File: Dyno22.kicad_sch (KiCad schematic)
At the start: 45 parts, among them J1 Pwr Input, J2 Display, J3 Pwr Output, J4 BPM & Sensors, J7 UART, U1 TS2937CW50, U2 LM324, U3 Demux

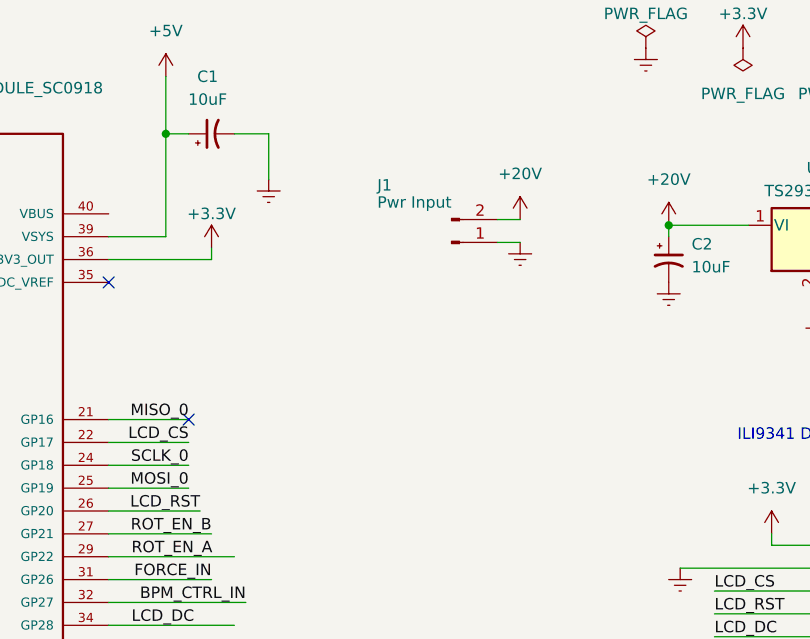
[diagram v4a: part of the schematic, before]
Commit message: Schematic modifications, including additional switch, fuse and LED
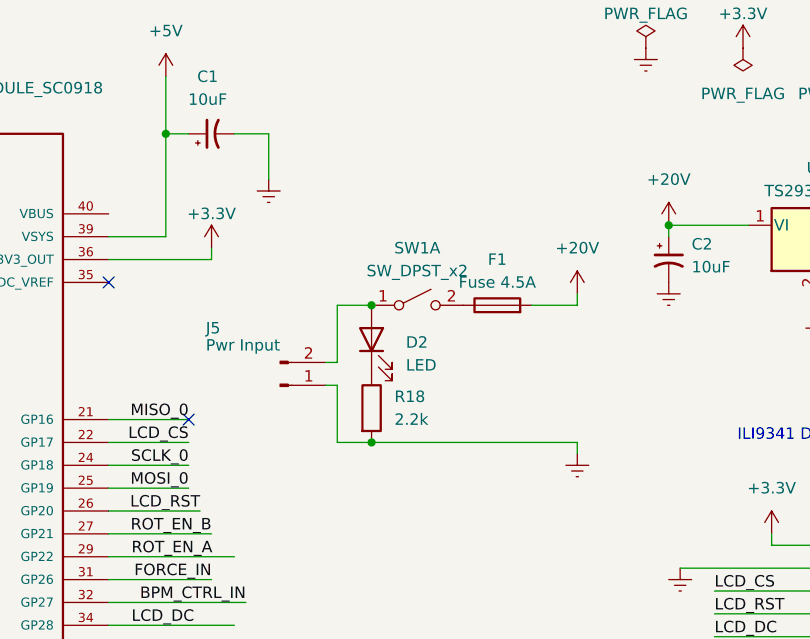
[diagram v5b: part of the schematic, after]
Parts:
- removed J1: Pwr Input, Connector_Molex:Molex_Nano-Fit_105313-xx02_1x02_P2.50mm_Horizontal, symbol Connector:Conn_01x02_Male
- added D2: LED, LED_SMD:LED_0603_1608Metric, symbol Device:LED
- added F1: Fuse 4.5A, symbol Device:Fuse
- added J5: Pwr Input, Connector_Molex:Molex_Nano-Fit_105313-xx02_1x02_P2.50mm_Horizontal, symbol Connector:Conn_01x02_Male
- added R18: 2.2k, Resistor_SMD:R_0402_1005Metric, symbol Device:R
- added SW1: SW_DPST_x2, symbol Switch:SW_DPST_x2
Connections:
- net +24V: now also F1.2
- net Earth: now also J5.1 (Pin_1), R18.2
- new net: D2.2 (A), J5.2 (Pin_2), SW1.1 (A)
- new net: F1.1, SW1.2 (B)
- new net: D2.1 (K), R18.1

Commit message: schematic changes v2
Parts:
- F1: footprint (none) -> Fuse:Fuse_1206_3216Metric
- SW1: footprint (none) -> Button_Switch_SMD:Nidec_Copal_SH-7040B
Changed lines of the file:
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@@
       (effects (font (size 1.27 1.27)))
     )
-    (property "Footprint" "" (at 115.57 48.26 0)
+    (property "Footprint" "Button_Switch_SMD:Nidec_Copal_SH-7040B" (at 115.57 48.26 0)
       (effects (font (size 1.27 1.27)) hide)
     )
@@
   )
   (symbol (lib_id "Connector:TestPoint") (at 69.85 186.69 0) (unit 1)
-    (in_bom yes) (on_board yes) (dnp no) (fields_autoplaced)
-    (property "Reference" "TP1" (at 72.39 182.118 0)
+    (in_bom yes) (on_board yes) (dnp no)
+    (property "Reference" "TP1" (at 73.66 182.88 0)
       (effects (font (size 1.27 1.27)) (justify left))
     )
@@
       (effects (font (size 1.27 1.27)))
     )
-    (property "Footprint" "" (at 124.46 50.038 90)
-      (effects (font (size 1.27 1.27)) hide)
-    )
-    (property "Datasheet" "~" (at 124.46 48.26 0)
-      (effects (font (size 1.27 1.27)) hide)
-    )
+    (property "Footprint" "Fuse:Fuse_1206_3216Metric" (at 124.46 50.038 90)
+      (effects (font (size 1.27 1.27)) hide)
+    )
+    (property "Datasheet" "https://www.digikey.ca/en/products/detail/eaton-electronics-division/CC12H4-5A-TR/2138898" (at 124.46 48.26 0)
+      (effects (font (size 1.27 1.27)) hide)
+    )

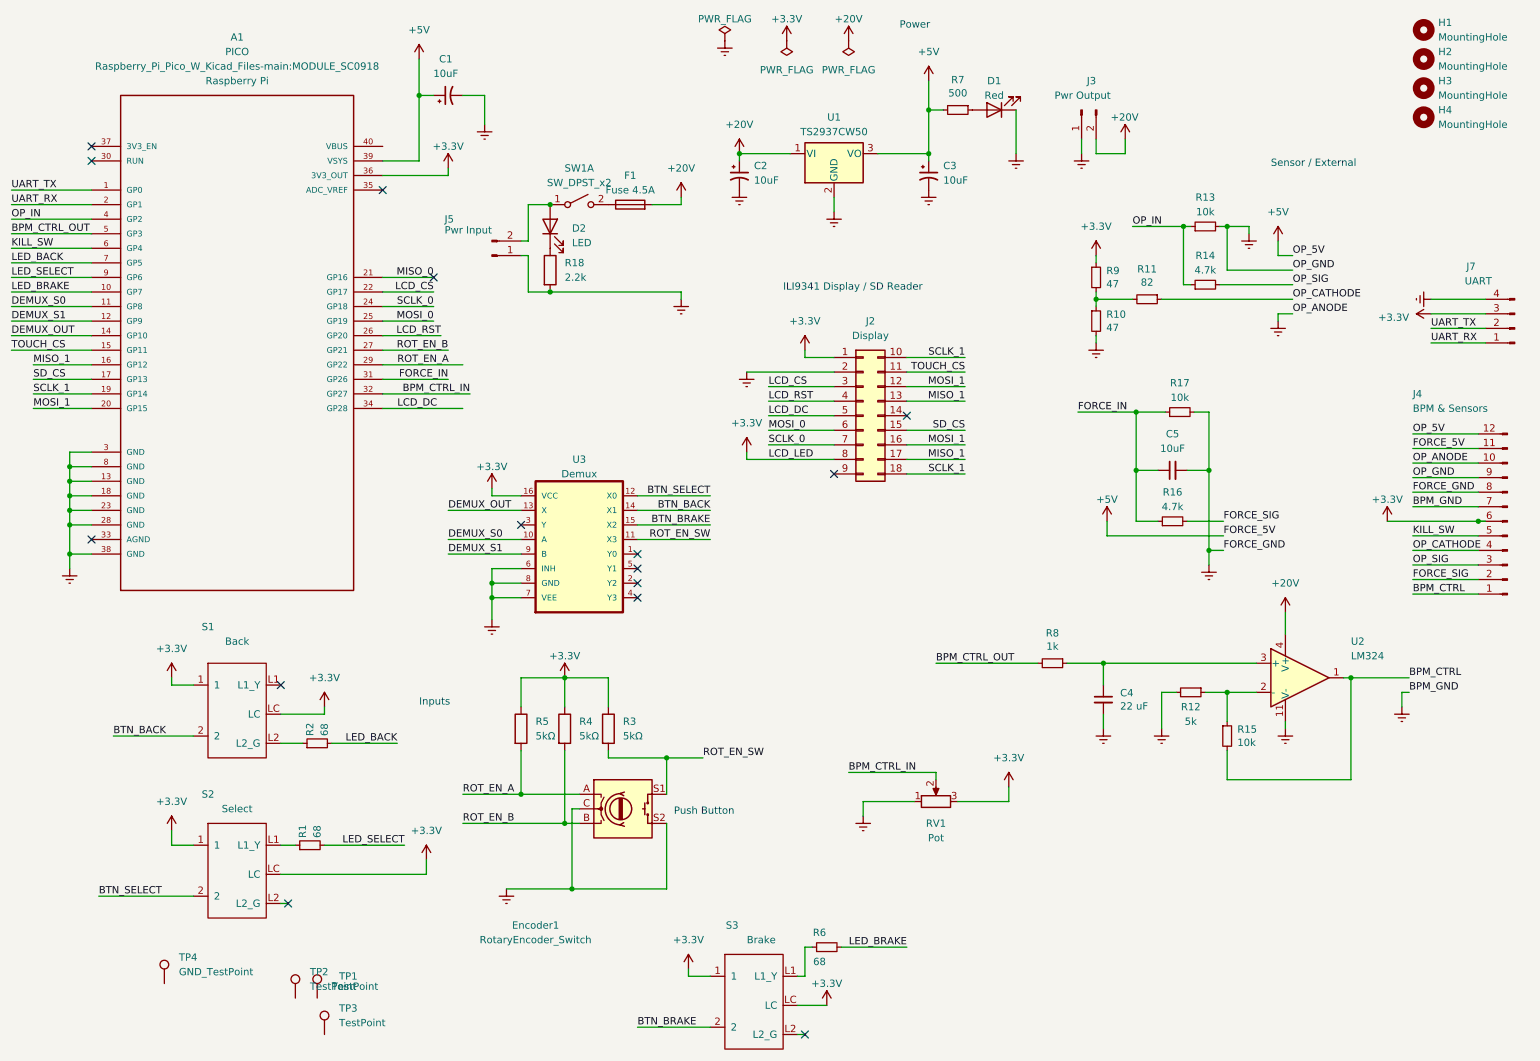
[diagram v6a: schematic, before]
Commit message: moved LCD PICO, updated traces for buttons encoder pot
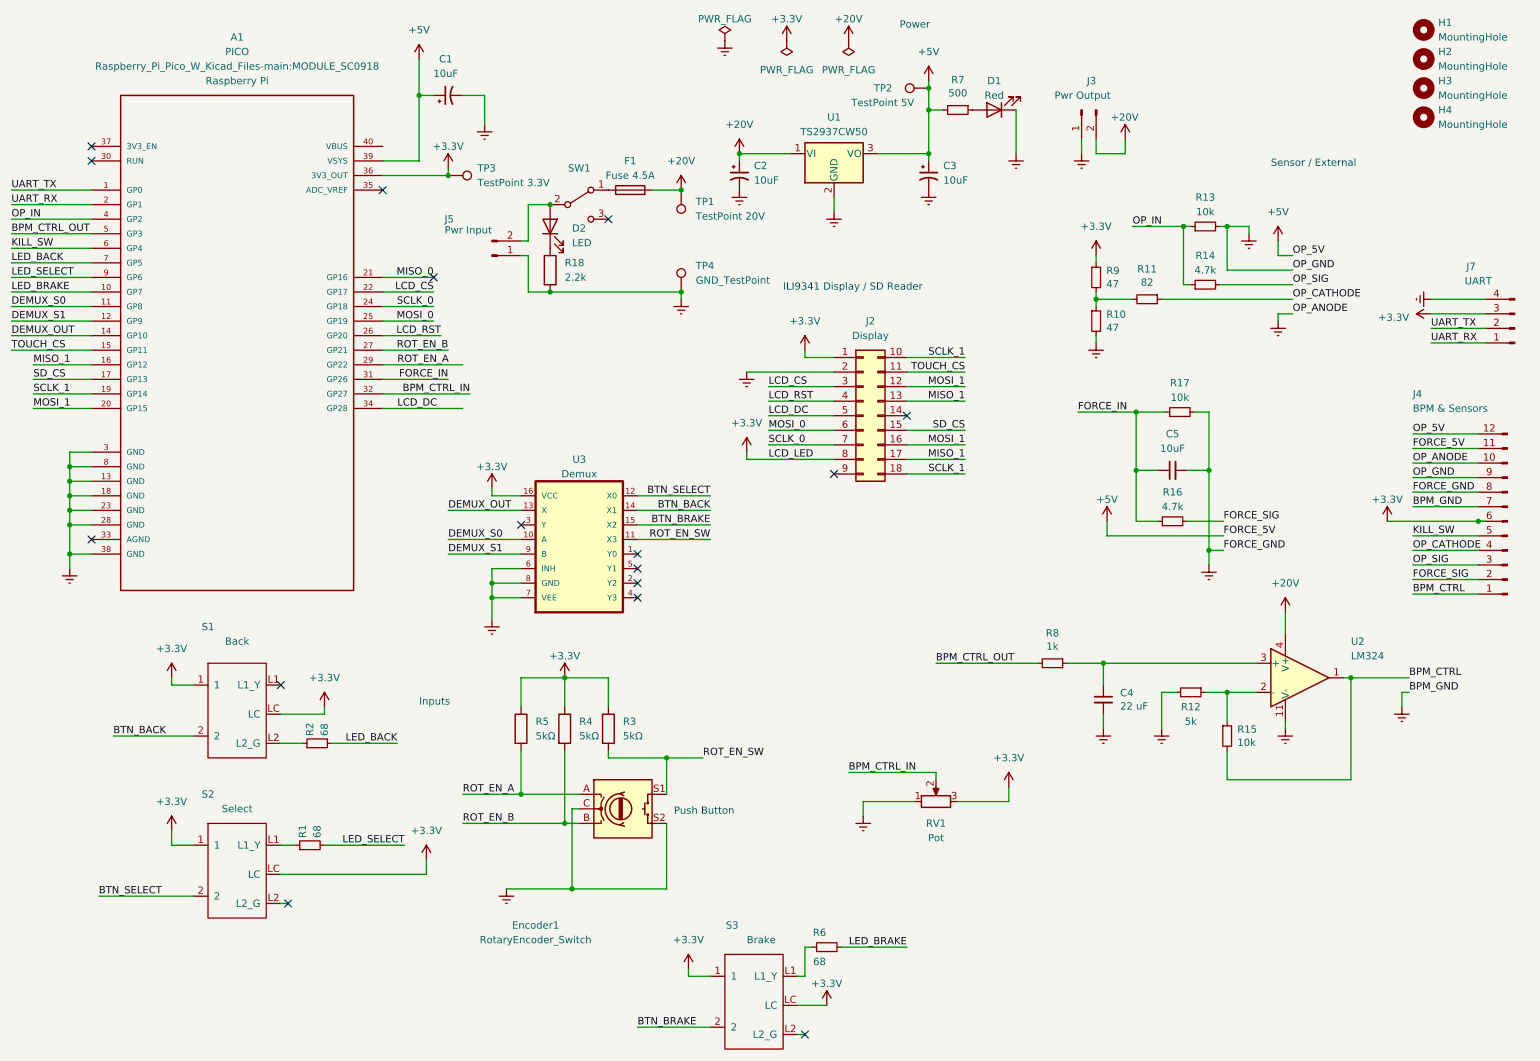
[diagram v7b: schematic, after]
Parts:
- RV1: footprint Potentiometer_THT:Potentiometer_Vishay_148-149_Single_Vertical_1 -> Potentiometer_THT:Potentiometer_Vishay_148-149_Single_Vertical
- SW1: footprint Button_Switch_SMD:Nidec_Copal_SH-7040B -> 300SP1J1BLKM2QE:SW_300SP1J1BLKM2QE; symbol Switch:SW_DPST_x2 -> Switch:SW_SPDT
- TP1: renamed from TP2; value TestPoint -> TestPoint 20V; footprint (none) -> TestPoint:TestPoint_Loop_D2.60mm_Drill1.4mm_Beaded
- TP2: renamed from TP1; value TestPoint -> TestPoint 5V; footprint (none) -> TestPoint:TestPoint_Loop_D2.60mm_Drill1.6mm_Beaded
- TP3: value TestPoint -> TestPoint 3.3V; footprint (none) -> TestPoint:TestPoint_Loop_D2.60mm_Drill1.6mm_Beaded
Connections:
- net +24V: now also TP1.1
- net +3.3V: now also TP3.1
- net +5V: now also TP2.1
- net Earth: now also TP4.1
- net at D2.2 (A), J5.2 (Pin_2): now also SW1.2 (B); no longer SW1.1 (A)
- net at F1.1: now also SW1.1 (A); no longer SW1.2 (B)
- no-connect marks 15 -> 16
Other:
- moved on the sheet: F1, TP1, TP2, TP3, TP4
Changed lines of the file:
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@@
   (junction (at 105.41 151.13) (diameter 0) (color 0 0 0 0)
   )
+  (junction (at 176.53 27.94) (diameter 0) (color 0 0 0 0)
+  )
   (junction (at 100.33 114.3) (diameter 0) (color 0 0 0 0)
   )
   (junction (at 143.51 39.37) (diameter 0) (color 0 0 0 0)
   )
+  (junction (at 92.71 43.18) (diameter 0) (color 0 0 0 0)
+  )
   (junction (at 113.03 156.21) (diameter 0) (color 0 0 0 0)
   )
@@
   (junction (at 26.67 104.14) (diameter 0) (color 0 0 0 0)
   )
+  (junction (at 133.35 63.5) (diameter 0) (color 0 0 0 0)
+  )
   (junction (at 220.98 52.07) (diameter 0) (color 0 0 0 0)
   )
@@
   (junction (at 228.6 52.07) (diameter 0) (color 0 0 0 0)
   )
+  (junction (at 133.35 45.72) (diameter 0) (color 0 0 0 0)
+  )
   (junction (at 250.19 130.81) (diameter 0) (color 0 0 0 0)
   )
   (no_connect (at 30.48 38.1))
   (no_connect (at 160.02 95.25))
+  (no_connect (at 120.65 50.8))
   (no_connect (at 63.5 132.08))
   (no_connect (at 105.41 104.14))
@@
     (stroke (width 0) (type default))
   )
-  (wire (pts (xy 133.35 48.26) (xy 133.35 46.99))
-    (stroke (width 0) (type default))
-  )
   (wire (pts (xy 212.725 84.455) (xy 212.725 94.615))
     (stroke (width 0) (type default))
@@
     (stroke (width 0) (type default))
   )
+  (wire (pts (xy 176.53 27.94) (xy 176.53 31.75))
+    (stroke (width 0) (type default))
+  )
   (wire (pts (xy 81.28 76.2) (xy 95.25 76.2))
     (stroke (width 0) (type default))
@@
     (stroke (width 0) (type default))
   )
+  (wire (pts (xy 128.27 45.72) (xy 133.35 45.72))
+    (stroke (width 0) (type default))
+  )
   (wire (pts (xy 92.71 41.91) (xy 92.71 43.18))
     (stroke (width 0) (type default))
@@
     (stroke (width 0) (type default))
   )
-  (wire (pts (xy 176.53 26.67) (xy 176.53 31.75))
+  (wire (pts (xy 176.53 26.67) (xy 176.53 27.94))
     (stroke (width 0) (type default))
   )
@@
     (stroke (width 0) (type default))
   )
-  (wire (pts (xy 128.27 48.26) (xy 133.35 48.26))
-    (stroke (width 0) (type default))
-  )
   (wire (pts (xy 190.5 149.86) (xy 190.5 152.4))
     (stroke (width 0) (type default))
@@
     )
   )
-  (symbol (lib_id "Switch:SW_DPST_x2") (at 115.57 48.26 0) (unit 1)
+  (symbol (lib_id "Switch:SW_SPDT") (at 115.57 48.26 0) (unit 1)
     (in_bom yes) (on_board yes) (dnp no) (fields_autoplaced)
     (property "Reference" "SW1" (at 115.57 41.91 0)
@@
     )
     (property "Value" "SW_DPST_x2" (at 115.57 44.45 0)
-      (effects (font (size 1.27 1.27)))
+      (effects (font (size 1.27 1.27)) hide)
     )
-    (property "Footprint" "Button_Switch_SMD:Nidec_Copal_SH-7040B" (at 115.57 48.26 0)
+    (property "Footprint" "300SP1J1BLKM2QE:SW_300SP1J1BLKM2QE" (at 115.57 48.26 0)
       (effects (font (size 1.27 1.27)) hide)
     )
@@
     (pin "2")
     (pin "3")
-    (pin "4")
     (instances
       (project "Dyno22"
@@
     )
   )
-  (symbol (lib_id "power:+20V") (at 133.35 46.99 0) (unit 1)
+  (symbol (lib_id "power:+20V") (at 133.35 45.72 0) (unit 1)
     (in_bom yes) (on_board yes) (dnp no) (fields_autoplaced)
-    (property "Reference" "#PWR010" (at 137.16 50.8 0)
+    (property "Reference" "#PWR010" (at 137.16 49.53 0)
       (effects (font (size 1.27 1.27)) hide)
     )
-    (property "Value" "+20V" (at 133.35 41.91 0)
+    (property "Value" "+20V" (at 133.35 40.64 0)
       (effects (font (size 1.27 1.27)))
     )
-    (property "Footprint" "" (at 133.35 46.99 0)
+    (property "Footprint" "" (at 133.35 45.72 0)
       (effects (font (size 1.27 1.27)) hide)
     )
-    (property "Datasheet" "" (at 133.35 46.99 0)
+    (property "Datasheet" "" (at 133.35 45.72 0)
       (effects (font (size 1.27 1.27)) hide)
     )
@@
     )
   )
-  (symbol (lib_id "Connector:TestPoint") (at 69.85 186.69 0) (unit 1)
+  (symbol (lib_id "Connector:TestPoint") (at 176.53 27.94 90) (unit 1)
     (in_bom yes) (on_board yes) (dnp no)
-    (property "Reference" "TP1" (at 73.66 182.88 0)
+    (property "Reference" "TP2" (at 170.18 27.94 90)
       (effects (font (size 1.27 1.27)) (justify left))
     )
-    (property "Value" "TestPoint" (at 72.39 184.658 0)
+    (property "Value" "TestPoint 5V" (at 173.99 30.48 90)
       (effects (font (size 1.27 1.27)) (justify left))
     )
-    (property "Footprint" "" (at 74.93 186.69 0)
+    (property "Footprint" "TestPoint:TestPoint_Loop_D2.60mm_Drill1.6mm_Beaded" (at 176.53 22.86 0)
       (effects (font (size 1.27 1.27)) hide)
     )
-    (property "Datasheet" "~" (at 74.93 186.69 0)
+    (property "Datasheet" "~" (at 176.53 22.86 0)
       (effects (font (size 1.27 1.27)) hide)
     )
@@
       (project "Dyno22"
         (path "/7271225a-6695-4332-8687-d26f1f45d708"
-          (reference "TP1") (unit 1)
+          (reference "TP2") (unit 1)
         )
       )
@@
     )
   )
-  (symbol (lib_id "Connector:TestPoint") (at 66.04 186.69 0) (unit 1)
+  (symbol (lib_id "Connector:TestPoint") (at 133.35 45.72 180) (unit 1)
     (in_bom yes) (on_board yes) (dnp no) (fields_autoplaced)
-    (property "Reference" "TP2" (at 68.58 182.118 0)
-      (effects (font (size 1.27 1.27)) (justify left))
+    (property "Reference" "TP1" (at 135.89 47.752 0)
+      (effects (font (size 1.27 1.27)) (justify right))
     )
-    (property "Value" "TestPoint" (at 68.58 184.658 0)
-      (effects (font (size 1.27 1.27)) (justify left))
+    (property "Value" "TestPoint 20V" (at 135.89 50.292 0)
+      (effects (font (size 1.27 1.27)) (justify right))
     )
-    (property "Footprint" "" (at 71.12 186.69 0)
+    (property "Footprint" "TestPoint:TestPoint_Loop_D2.60mm_Drill1.4mm_Beaded" (at 128.27 45.72 0)
       (effects (font (size 1.27 1.27)) hide)
     )
-    (property "Datasheet" "~" (at 71.12 186.69 0)
+    (property "Datasheet" "~" (at 128.27 45.72 0)
       (effects (font (size 1.27 1.27)) hide)
     )
@@
       (project "Dyno22"
         (path "/7271225a-6695-4332-8687-d26f1f45d708"
-          (reference "TP2") (unit 1)
+          (reference "TP1") (unit 1)
         )
       )
@@
     )
   )
-  (symbol (lib_id "Connector:TestPoint") (at 71.12 193.04 0) (unit 1)
+  (symbol (lib_id "Connector:TestPoint") (at 92.71 43.18 270) (unit 1)
     (in_bom yes) (on_board yes) (dnp no) (fields_autoplaced)
-    (property "Reference" "TP3" (at 73.66 188.468 0)
+    (property "Reference" "TP3" (at 97.79 41.91 90)
       (effects (font (size 1.27 1.27)) (justify left))
     )
-    (property "Value" "TestPoint" (at 73.66 191.008 0)
+    (property "Value" "TestPoint 3.3V" (at 97.79 44.45 90)
       (effects (font (size 1.27 1.27)) (justify left))
     )
-    (property "Footprint" "" (at 76.2 193.04 0)
+    (property "Footprint" "TestPoint:TestPoint_Loop_D2.60mm_Drill1.6mm_Beaded" (at 92.71 48.26 0)
       (effects (font (size 1.27 1.27)) hide)
     )
-    (property "Datasheet" "~" (at 76.2 193.04 0)
+    (property "Datasheet" "~" (at 92.71 48.26 0)
       (effects (font (size 1.27 1.27)) hide)
     )
@@
       (effects (font (size 1.27 1.27)))
     )
-    (property "Footprint" "Potentiometer_THT:Potentiometer_Vishay_148-149_Single_Vertical_1" (at 177.8 152.4 0)
+    (property "Footprint" "Potentiometer_THT:Potentiometer_Vishay_148-149_Single_Vertical" (at 177.8 152.4 0)
       (effects (font (size 1.27 1.27)) hide)
     )
@@
     )
   )
-  (symbol (lib_id "Device:Fuse") (at 124.46 48.26 90) (unit 1)
+  (symbol (lib_id "Device:Fuse") (at 124.46 45.72 90) (unit 1)
     (in_bom yes) (on_board yes) (dnp no) (fields_autoplaced)
-    (property "Reference" "F1" (at 124.46 43.18 90)
+    (property "Reference" "F1" (at 124.46 40.64 90)
       (effects (font (size 1.27 1.27)))
     )
-    (property "Value" "Fuse 4.5A" (at 124.46 45.72 90)
+    (property "Value" "Fuse 4.5A" (at 124.46 43.18 90)
       (effects (font (size 1.27 1.27)))
     )
-    (property "Footprint" "Fuse:Fuse_1206_3216Metric" (at 124.46 50.038 90)
+    (property "Footprint" "Fuse:Fuse_1206_3216Metric" (at 124.46 47.498 90)
       (effects (font (size 1.27 1.27)) hide)
     )
-    (property "Datasheet" "https://www.digikey.ca/en/products/detail/eaton-electronics-division/CC12H4-5A-TR/2138898" (at 124.46 48.26 0)
+    (property "Datasheet" "https://www.digikey.ca/en/products/detail/eaton-electronics-division/CC12H4-5A-TR/2138898" (at 124.46 45.72 0)
       (effects (font (size 1.27 1.27)) hide)
     )
@@
     )
   )
-  (symbol (lib_id "Connector:TestPoint") (at 43.18 184.15 0) (unit 1)
+  (symbol (lib_id "Connector:TestPoint") (at 133.35 63.5 0) (unit 1)
     (in_bom yes) (on_board yes) (dnp no) (fields_autoplaced)
-    (property "Reference" "TP4" (at 45.72 179.578 0)
+    (property "Reference" "TP4" (at 135.89 58.928 0)
       (effects (font (size 1.27 1.27)) (justify left))
     )
-    (property "Value" "GND_TestPoint" (at 45.72 182.118 0)
+    (property "Value" "GND_TestPoint" (at 135.89 61.468 0)
       (effects (font (size 1.27 1.27)) (justify left))
     )
-    (property "Footprint" "TestPoint:TestPoint_Pad_4.0x4.0mm" (at 48.26 184.15 0)
+    (property "Footprint" "TestPoint:TestPoint_Pad_4.0x4.0mm" (at 138.43 63.5 0)
       (effects (font (size 1.27 1.27)) hide)
     )
-    (property "Datasheet" "~" (at 48.26 184.15 0)
+    (property "Datasheet" "~" (at 138.43 63.5 0)
       (effects (font (size 1.27 1.27)) hide)
     )
